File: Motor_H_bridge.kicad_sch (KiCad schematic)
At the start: 0 parts

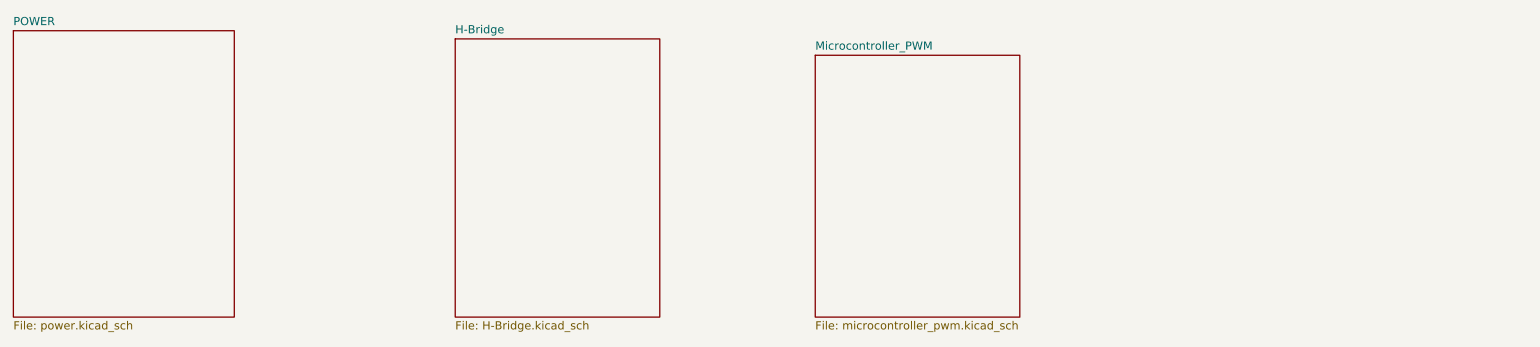
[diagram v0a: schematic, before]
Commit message: Done upto shunt circuit, H-bridge, remaining Loogic
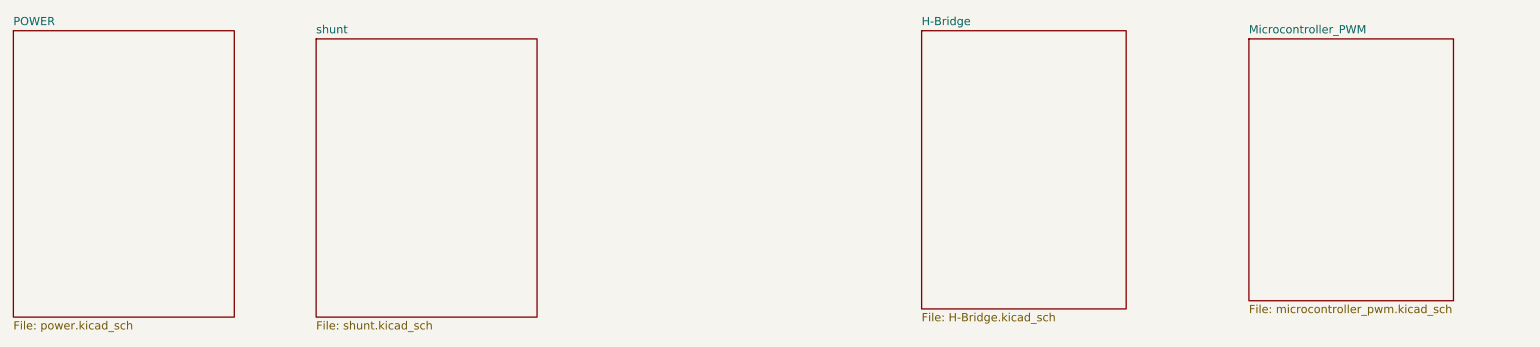
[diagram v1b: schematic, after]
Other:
- added sheet shunt (shunt.kicad_sch)
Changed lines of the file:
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@@
 	(paper "A4")
 	(sheet
-		(at 106.68 40.64)
+		(at 85.09 40.64)
+		(size 34.29 43.18)
+		(fields_autoplaced yes)
+		(stroke
+			(width 0.1524)
+			(type solid)
+		)
+		(fill
+			(color 0 0 0 0.0000)
+		)
+		(property "Sheetname" "shunt"
+			(at 85.09 39.9284 0)
+			(effects
+				(font
+					(size 1.27 1.27)
+				)
+				(justify left bottom)
+			)
+		)
+		(property "Sheetfile" "shunt.kicad_sch"
+			(at 85.09 84.4046 0)
+			(effects
+				(font
+					(size 1.27 1.27)
+				)
+				(justify left top)
+			)
+		)
+		(instances
+			(project "Motor_H_bridge"
+				(path "/fc60c7e1-3603-4753-a333-d4a66d2fbdcd"
+					(page "5")
+				)
+			)
+		)
+	)
+	(sheet
+		(at 179.07 39.37)
 		(size 31.75 43.18)
 		(fields_autoplaced yes)
@@
 		)
 		(property "Sheetname" "H-Bridge"
-			(at 106.68 39.9284 0)
+			(at 179.07 38.6584 0)
 			(effects
 				(font
@@
 		)
 		(property "Sheetfile" "H-Bridge.kicad_sch"
-			(at 106.68 84.4046 0)
+			(at 179.07 83.1346 0)
 			(effects
 				(font
@@
 	)
 	(sheet
-		(at 162.56 43.18)
+		(at 229.87 40.64)
 		(size 31.75 40.64)
 		(fields_autoplaced yes)
@@
 		)
 		(property "Sheetname" "Microcontroller_PWM"
-			(at 162.56 42.4684 0)
+			(at 229.87 39.9284 0)
 			(effects
 				(font
@@
 		)
 		(property "Sheetfile" "microcontroller_pwm.kicad_sch"
-			(at 162.56 84.4046 0)
+			(at 229.87 81.8646 0)
 			(effects
 				(font

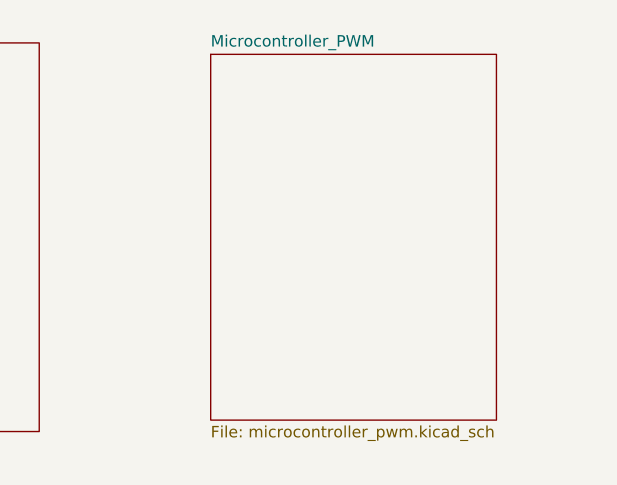
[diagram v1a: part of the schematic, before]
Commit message: Finished all parts of schematic: power, H-bridge, logic and shunt schematics
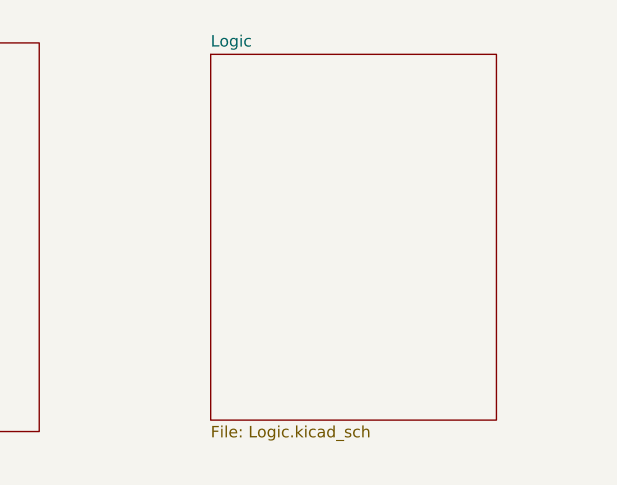
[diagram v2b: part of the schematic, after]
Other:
- sheet Microcontroller_PWM renamed Logic
- sheet Logic: file microcontroller_pwm.kicad_sch -> Logic.kicad_sch
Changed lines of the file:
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@@
 			(color 0 0 0 0.0000)
 		)
-		(property "Sheetname" "Microcontroller_PWM"
+		(property "Sheetname" "Logic"
 			(at 229.87 39.9284 0)
 			(effects
@@
 			)
 		)
-		(property "Sheetfile" "microcontroller_pwm.kicad_sch"
+		(property "Sheetfile" "Logic.kicad_sch"
 			(at 229.87 81.8646 0)
 			(effects
